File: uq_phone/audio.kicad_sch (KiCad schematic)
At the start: 34 parts, among them J10 SJ-3551B-MSMT-TR-67, J11 Conn_01x02, U13 TS3A5018RSVR, U14 NAU88C22YG

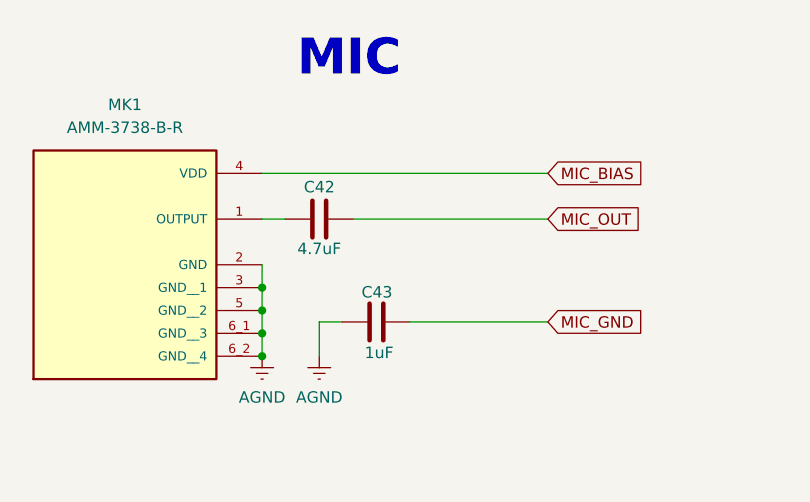
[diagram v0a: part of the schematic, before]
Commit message: Clean up and add DNP
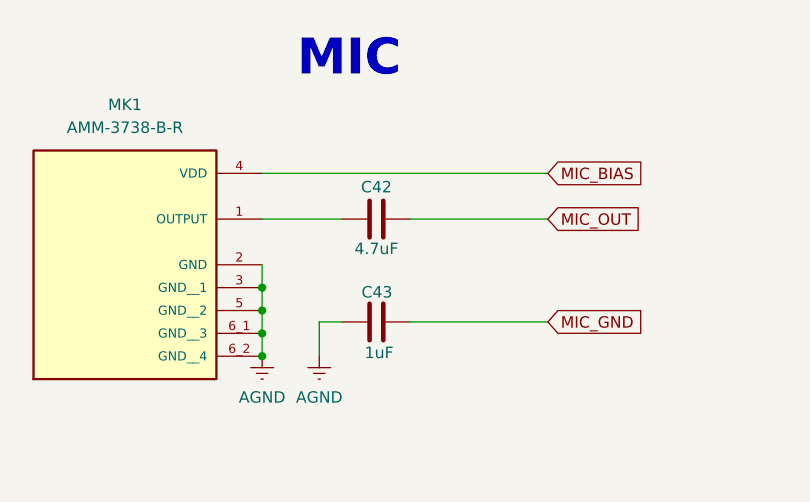
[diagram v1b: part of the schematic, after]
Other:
- moved on the sheet: C42
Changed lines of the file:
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@@
 	(wire
 		(pts
-			(xy 271.78 48.26) (xy 293.37 48.26)
+			(xy 278.13 48.26) (xy 293.37 48.26)
 		)
 		(stroke
@@
 	(wire
 		(pts
-			(xy 261.62 48.26) (xy 264.16 48.26)
+			(xy 261.62 48.26) (xy 270.51 48.26)
 		)
 		(stroke
@@
 	(symbol
 		(lib_id "Capacitors:Capacitor_4.7uF")
-		(at 267.97 48.26 90)
+		(at 274.32 48.26 90)
 		(unit 1)
 		(exclude_from_sim no)
@@
 		(dnp no)
 		(property "Reference" "C42"
-			(at 267.97 44.704 90)
+			(at 274.32 44.704 90)
 			(effects
 				(font
@@
 		)
 		(property "Value" "4.7uF"
-			(at 267.97 51.562 90)
+			(at 274.32 51.562 90)
 			(effects
 				(font
@@
 		)
 		(property "Footprint" "Capacitor_SMD:C_0402_1005Metric"
-			(at 267.97 48.26 0)
+			(at 274.32 48.26 0)
 			(effects
 				(font
@@
 		)
 		(property "Datasheet" ""
-			(at 267.97 48.26 0)
+			(at 274.32 48.26 0)
 			(effects
 				(font
@@
 		)
 		(property "Description" "4.7 µF ±10% 6.3V Ceramic Capacitor X5R 0402 (1005 Metric)"
-			(at 267.97 48.26 0)
+			(at 274.32 48.26 0)
 			(effects
 				(font

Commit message: Update Various Connectors
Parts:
- added SP1: AS01808AO-3-R, symbol Misc:Speaker
- R38: footprint Resistor_SMD:R_0603_1608Metric -> Resistor_SMD:R_0402_1005Metric
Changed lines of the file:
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@@
 	(text "Suitable for 8-Ohm 1W"
 		(exclude_from_sim no)
-		(at 71.374 65.278 0)
+		(at 87.884 56.642 0)
 		(effects
 			(font
@@
 	)
 	(symbol
-		(lib_id "Resistors:Resistor_2k2")
-		(at 77.47 234.95 0)
-		(unit 1)
-		(exclude_from_sim no)
-		(in_bom yes)
-		(on_board yes)
-		(dnp no)
-		(fields_autoplaced yes)
-		(property "Reference" "R38"
-			(at 80.01 233.6799 0)
-			(effects
-				(font
-					(size 1.27 1.27)
-				)
-				(justify left)
-			)
-		)
-		(property "Value" "2.2k"
-			(at 80.01 236.2199 0)
-			(effects
-				(font
-					(size 1.27 1.27)
-				)
-				(justify left)
-			)
-		)
-		(property "Footprint" "Resistor_SMD:R_0603_1608Metric"
-			(at 77.47 238.76 0)
-			(effects
-				(font
-					(size 1.27 1.27)
-				)
-				(hide yes)
-			)
-		)
-		(property "Datasheet" ""
-			(at 77.47 238.76 0)
-			(effects
-				(font
-					(size 1.27 1.27)
-				)
-				(hide yes)
-			)
-		)
-		(property "Description" ""
-			(at 77.47 238.76 0)
-			(effects
-				(font
-					(size 1.27 1.27)
-				)
-				(hide yes)
-			)
-		)
-		(pin "2"
-		)
-		(pin "1"
-		)
-		(instances
-			(project "uq_phone"
-				(path "/14f57415-6807-40a5-bb38-3cb818a2cdae/e19f4f8c-44cb-4a36-b4d3-60ff6ff42a2f"
-					(reference "R38")
-					(unit 1)
-				)
-			)
-		)
-	)
-	(symbol
 		(lib_id "Resistors:Resistor_0R")
 		(at 81.28 173.99 90)
@@
 	)
 	(symbol
+		(lib_id "Resistors:Resistor_2k2")
+		(at 77.47 234.95 0)
+		(unit 1)
+		(exclude_from_sim no)
+		(in_bom yes)
+		(on_board yes)
+		(dnp no)
+		(fields_autoplaced yes)
+		(property "Reference" "R38"
+			(at 80.01 233.6799 0)
+			(effects
+				(font
+					(size 1.27 1.27)
+				)
+				(justify left)
+			)
+		)
+		(property "Value" "2.2k"
+			(at 80.01 236.2199 0)
+			(effects
+				(font
+					(size 1.27 1.27)
+				)
+				(justify left)
+			)
+		)
+		(property "Footprint" "Resistor_SMD:R_0402_1005Metric"
+			(at 77.47 238.76 0)
+			(effects
+				(font
+					(size 1.27 1.27)
+				)
+				(hide yes)
+			)
+		)
+		(property "Datasheet" ""
+			(at 77.47 238.76 0)
+			(effects
+				(font
+					(size 1.27 1.27)
+				)
+				(hide yes)
+			)
+		)
+		(property "Description" "RES 2.2K OHM 5% 1/16W 0402"
+			(at 77.47 238.76 0)
+			(effects
+				(font
+					(size 1.27 1.27)
+				)
+				(hide yes)
+			)
+		)
+		(pin "2"
+		)
+		(pin "1"
+		)
+		(instances
+			(project ""
+				(path "/14f57415-6807-40a5-bb38-3cb818a2cdae/e19f4f8c-44cb-4a36-b4d3-60ff6ff42a2f"
+					(reference "R38")
+					(unit 1)
+				)
+			)
+		)
+	)
+	(symbol
 		(lib_id "power:GNDREF")
 		(at 307.34 222.25 0)
@@
 					(unit 1)
 				)
+			)
+		)
+	)
+	(symbol
+		(lib_id "Misc:Speaker")
+		(at 114.3 48.26 0)
+		(unit 1)
+		(exclude_from_sim no)
+		(in_bom yes)
+		(on_board no)
+		(dnp no)
+		(fields_autoplaced yes)
+		(property "Reference" "SP1"
+			(at 118.11 46.9899 0)
+			(effects
+				(font
+					(size 1.27 1.27)
+				)
+				(justify left)
+			)
+		)
+		(property "Value" "AS01808AO-3-R"
+			(at 118.11 49.5299 0)
+			(effects
+				(font
+					(size 1.27 1.27)
+				)
+				(justify left)
+			)
+		)
+		(property "Footprint" ""
+			(at 114.3 48.26 0)
+			(effects
+				(font
+					(size 1.27 1.27)
+				)
+				(hide yes)
+			)
+		)
+		(property "Datasheet" ""
+			(at 114.3 48.26 0)
+			(effects
+				(font
+					(size 1.27 1.27)
+				)
+				(hide yes)
+			)
+		)
+		(property "Description" "https://www.digikey.com.au/en/products/detail/pui-audio-inc/AS01808AO-3-R/5977706"
+			(at 113.03 43.688 0)
+			(effects
+				(font
+					(size 1.27 1.27)
+				)
+				(hide yes)
+			)
+		)
+		(instances
+			(project ""
+				(path "/14f57415-6807-40a5-bb38-3cb818a2cdae/e19f4f8c-44cb-4a36-b4d3-60ff6ff42a2f"
+					(reference "SP1")
+					(unit 1)
+				)

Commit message: Generate Early production outputs
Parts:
- C36: LCSC PN (none) -> C307331
- C37, C38, C39, C41, C43: LCSC PN (none) -> C52923
- C40: LCSC PN (none) -> C70465
- C42, C44, C45, C46, C47, C48, C49: LCSC PN (none) -> C191541
- FB1, FB2: LCSC PN (none) -> C76818
- MK1: Description_1 4X3MM MEMS MIC 20~20KHZ 38DB -> 4X3MM MEMS MIC 20~20KHZ 38DB
- R35, R36, R39, R44: LCSC PN (none) -> C851848
- R37, R40, R41, R42, R43, R46, R47: LCSC PN (none) -> C95177
- R38: LCSC PN (none) -> C606171
- R45: LCSC PN (none) -> C427250
- SP1: now not fitted
- U13: LCSC PN (none) -> C201641
